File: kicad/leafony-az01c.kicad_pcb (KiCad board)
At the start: 4 copper layers, 20 x 20 mm, 22 parts, among them CN1 Leafony Bus, J1 CX90M-16P, U1 TS3A4751RUCR, U2 USBLC6-2P6, U3 FT234XD, U4 TPS6282533DMQR

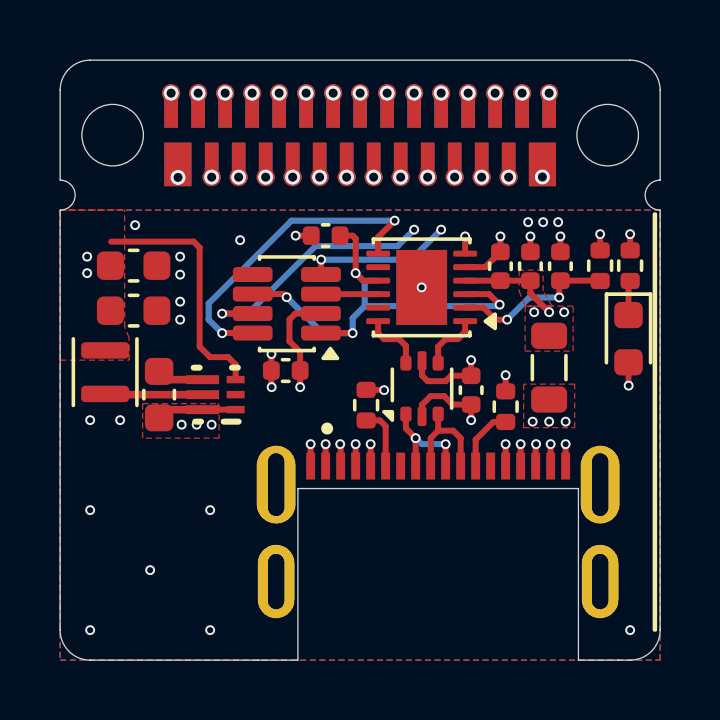
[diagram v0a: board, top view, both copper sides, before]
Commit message: BOMとガーバーを更新
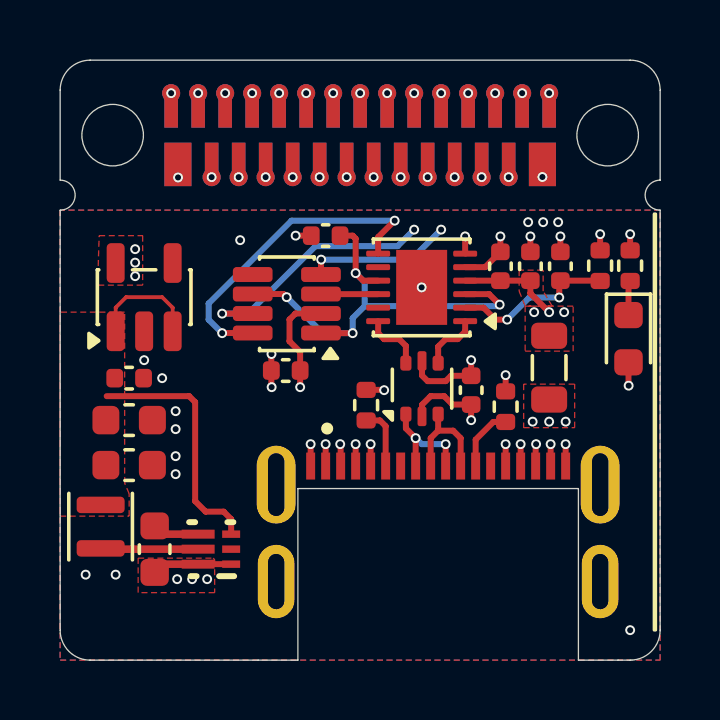
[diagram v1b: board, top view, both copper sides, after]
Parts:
- added C10: 0.1uF(K)/50V/X5R, Capacitor_SMD:C_0402_1005Metric, F.Cu at (27.3, 35.6)
- added U5: MAX40200AUK+T, Package_TO_SOT_SMD:SOT-23-5, F.Cu at (27.8, 32.9)
- U1: value TS3A4751RUCR -> TS3A4741DCNR
- moved C7 5.15 mm to (28.1, 41.3)
- moved C8 5.15 mm to (27.3, 38.5)
- moved C9 5.15 mm to (27.3, 37.0)
- moved L1 5.15 mm to (26.4, 40.5)
- moved U4 5.15 mm to (30.0, 41.3)
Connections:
- C8 pad 1: +3V3 -> Net-(U4-FB)
- C9 pad 1: +3V3 -> Net-(U4-FB)
- L1 pad 2: +3V3 -> Net-(U4-FB)
- U4 pad 3: +3V3 -> Net-(U4-FB)
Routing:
- net +3V3: track 17.2 -> 3.53 mm, vias 4 -> 5
- net Net-(U4-FB): track 0.00 -> 12.0 mm
- net VBUS: track 30.4 -> 34.9 mm
- net GND: vias 34 -> 30
- added copper zone on F.Cu, net Net-(U4-FB)
